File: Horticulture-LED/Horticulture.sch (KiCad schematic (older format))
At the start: 66 parts, among them J3 Conn_01x04_Male, J4 Conn_01x04_Male, U1 TLE4309, U2 TLE4309, U3 TLE4309, U4 TLE4309, U5 PCA9633DP2

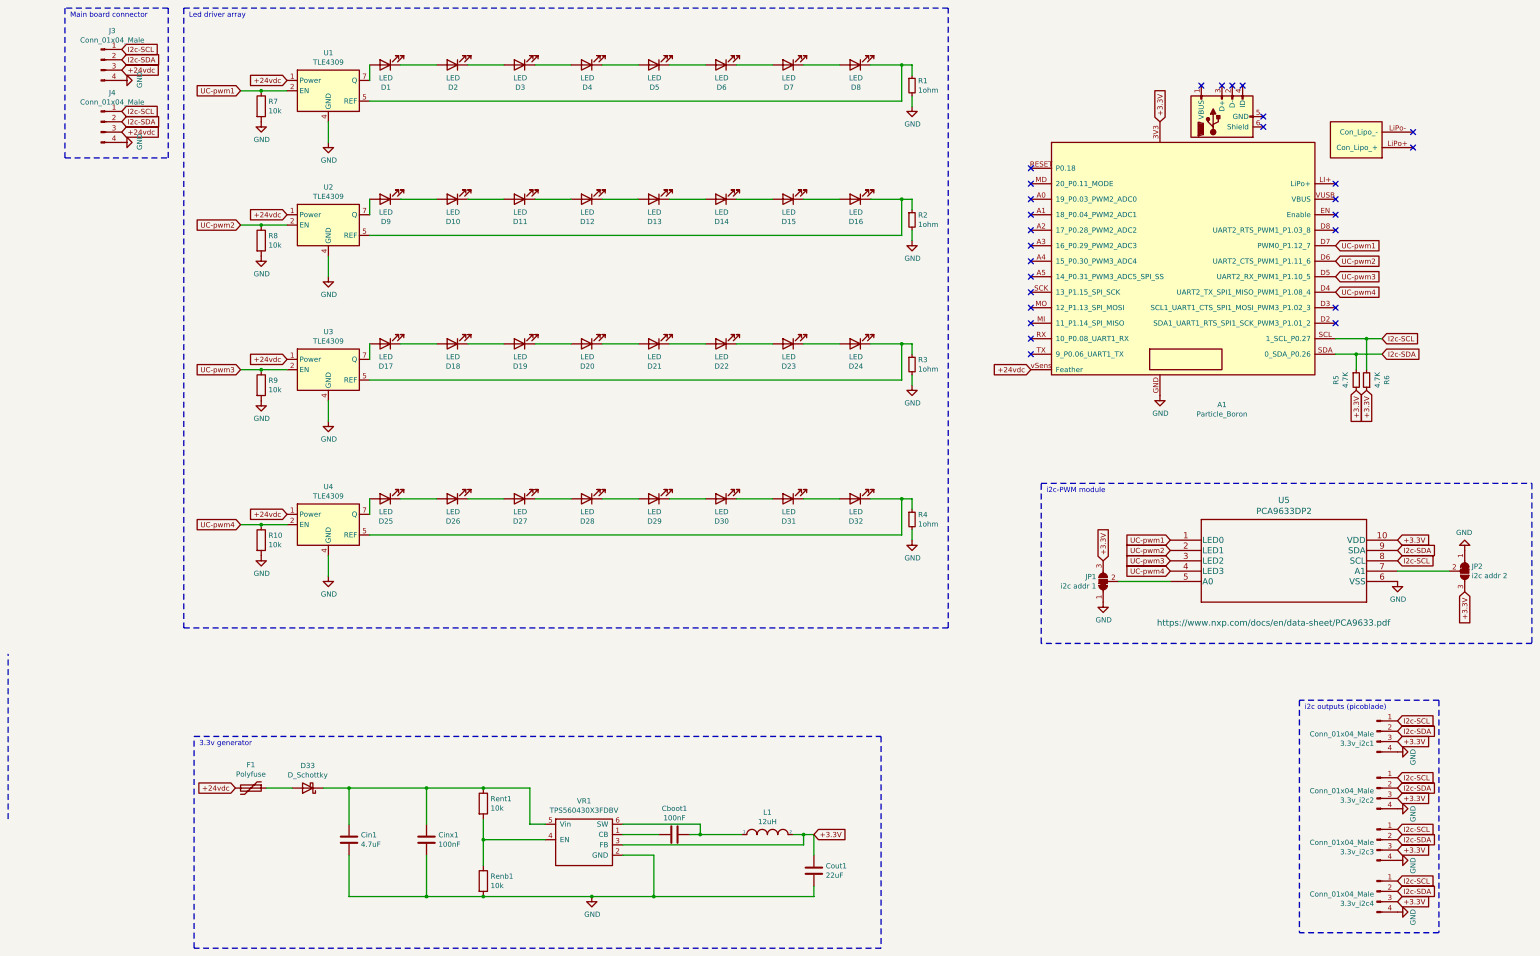
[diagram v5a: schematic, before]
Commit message: ryddet i resistorer
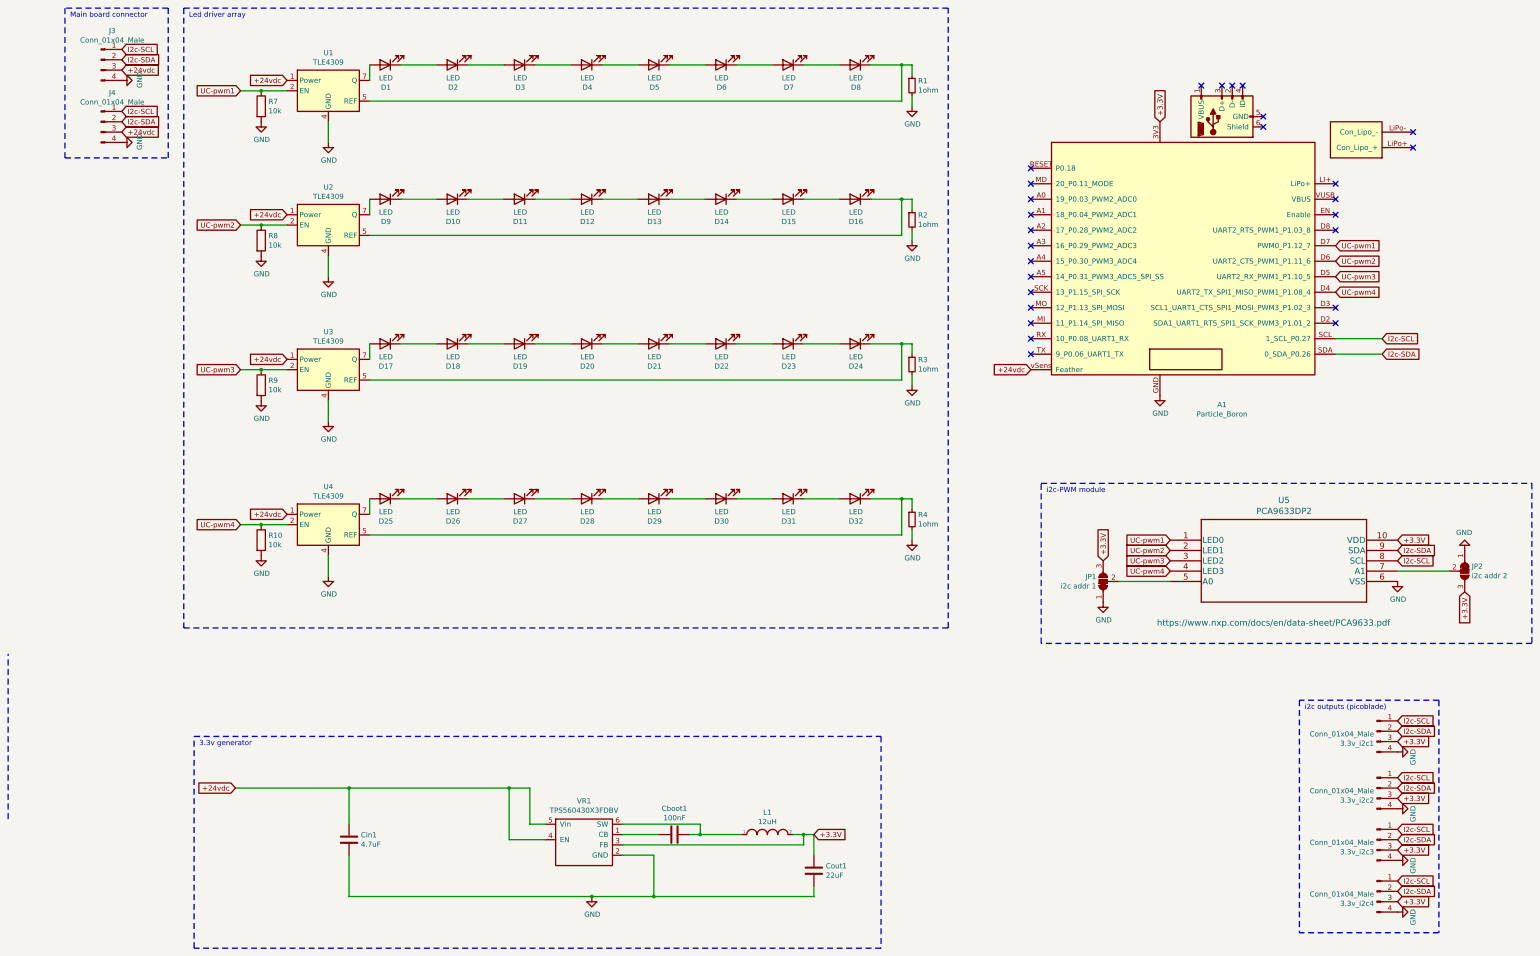
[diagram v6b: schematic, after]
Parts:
- removed Cinx1: 100nF, Capacitor_SMD:C_0603_1608Metric, symbol Device:C
- removed D33: D_Schottky, Diode_SMD:D_SOD-323, symbol Device:D_Schottky
- removed F1: Polyfuse, Fuse:Fuse_1206_3216Metric, symbol Device:Polyfuse
- removed R5, R6: 4.7K, Resistor_SMD:R_0402_1005Metric, symbol Device:R_Small
- removed Renb1, Rent1: 10k, Resistor_SMD:R_0402_1005Metric, symbol Device:R
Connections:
- net +24vdc: now also Cin1.1, VR1.4 (EN), VR1.5 (Vin)
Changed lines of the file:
@@
 Connection ~ 9100 5500
-$Comp
-L particle:Particle_Boron A1
-U 1 1 5EF20E12
-P 11800 3050
-F 0 "A1" H 12200 1511 50  0000 C CNN
-F 1 "Particle_Boron" H 12200 1420 50  0000 C CNN
-F 2 "Adafruit_FeatherWing:PCB_FeatherWing" H 11100 3250 50  0001 C CNN
-F 3 "" H 11100 3250 50  0001 C CNN
-	1    11800 3050
-	1    0    0    -1
-$EndComp
 $Comp
 L Connector:Conn_01x04_Male J3
@@
 +3.3V
 $Comp
-L Device:R_Small R5
-U 1 1 5F25CC3B
-P 13500 4350
-F 0 "R5" V 13304 4350 50  0000 C CNN
-F 1 "4.7K" V 13395 4350 50  0000 C CNN
-F 2 "Resistor_SMD:R_0402_1005Metric" H 13500 4350 50  0001 C CNN
-F 3 "~" H 13500 4350 50  0001 C CNN
-	1    13500 4350
-	1    0    0    -1
-$EndComp
-$Comp
-L Device:R_Small R6
-U 1 1 5F25F078
-P 13600 4350
-F 0 "R6" V 13404 4350 50  0000 C CNN
-F 1 "4.7K" V 13495 4350 50  0000 C CNN
-F 2 "Resistor_SMD:R_0402_1005Metric" H 13600 4350 50  0001 C CNN
-F 3 "~" H 13600 4350 50  0001 C CNN
-	1    13600 4350
-	-1   0    0    1
-$EndComp
-Wire Wire Line
-	13600 4250 13600 3950
-Connection ~ 13600 3950
-Wire Wire Line
-	13600 3950 13750 3950
-Wire Wire Line
-	13500 4250 13500 4100
-Connection ~ 13500 4100
-Wire Wire Line
-	13500 4100 13750 4100
-Text GLabel 13500 4450 3    50   Input ~ 0
-+3.3V
-Text GLabel 13600 4450 3    50   Input ~ 0
-+3.3V
-$Comp
 L Connector:Conn_01x04_Male J4
 U 1 1 5F2EA6B4
@@
 Text GLabel 8250 8750 2    50   Input ~ 0
 +3.3V
-Connection ~ 5050 8800
-Wire Wire Line
-	5050 8800 5050 9050
-Wire Wire Line
-	5050 8600 5050 8800
-Wire Wire Line
-	5650 8800 5050 8800
 Wire Wire Line
 	6700 9350 8250 9350
@@
 Wire Wire Line
 	8050 8750 8150 8750
-Connection ~ 5050 9350
 Wire Wire Line
 	8250 9350 8250 9250
 Wire Wire Line
-	5050 9350 6100 9350
-Wire Wire Line
 	7050 8750 7150 8750
 Wire Wire Line
-	4500 9350 3750 9350
-Connection ~ 4500 9350
-Wire Wire Line
-	4500 8950 4500 9350
-Wire Wire Line
 	3750 9350 3750 8950
 Wire Wire Line
-	5050 9350 4500 9350
-Wire Wire Line
-	4500 8300 3750 8300
-Connection ~ 4500 8300
-Wire Wire Line
-	4500 8650 4500 8300
-Connection ~ 5050 8300
-Wire Wire Line
 	3750 8300 3750 8650
 Wire Wire Line
-	5050 8300 4500 8300
-Wire Wire Line
-	5500 8300 5050 8300
+	5500 8300 5300 8300
 Wire Wire Line
 	5500 8650 5500 8300
 Wire Wire Line
 	5650 8650 5500 8650
-$Comp
-L Device:R Renb1
-U 1 1 5F7D2821
-P 5050 9200
-F 0 "Renb1" H 5120 9246 50  0000 L CNN
-F 1 "10k" H 5120 9155 50  0000 L CNN
-F 2 "Resistor_SMD:R_0402_1005Metric" V 4980 9200 50  0001 C CNN
-F 3 "~" H 5050 9200 50  0001 C CNN
-	1    5050 9200
-	1    0    0    -1
-$EndComp
-$Comp
-L Device:R Rent1
-U 1 1 5F7D0EBB
-P 5050 8450
-F 0 "Rent1" H 5120 8496 50  0000 L CNN
-F 1 "10k" H 5120 8405 50  0000 L CNN
-F 2 "Resistor_SMD:R_0402_1005Metric" V 4980 8450 50  0001 C CNN
-F 3 "~" H 5050 8450 50  0001 C CNN
-	1    5050 8450
-	1    0    0    -1
-$EndComp
 $Comp
 L pspice:INDUCTOR L1
@@
 $EndComp
 $Comp
-L Device:C Cinx1
-U 1 1 5F7BFD6B
-P 4500 8800
-F 0 "Cinx1" H 4615 8846 50  0000 L CNN
-F 1 "100nF" H 4615 8755 50  0000 L CNN
-F 2 "Capacitor_SMD:C_0603_1608Metric" H 4538 8650 50  0001 C CNN
-F 3 "~" H 4500 8800 50  0001 C CNN
-	1    4500 8800
-	1    0    0    -1
-$EndComp
-$Comp
 L Device:C Cin1
 U 1 1 5F7BEDEC
@@
 Wire Notes Line
 	450  8600 450  7000
-$Comp
-L Device:Polyfuse F1
-U 1 1 5F8B0FBE
-P 2800 8300
-F 0 "F1" V 2575 8300 50  0000 C CNN
-F 1 "Polyfuse" V 2666 8300 50  0000 C CNN
-F 2 "Fuse:Fuse_1206_3216Metric" H 2850 8100 50  0001 L CNN
-F 3 "~" H 2800 8300 50  0001 C CNN
-	1    2800 8300
-	0    1    1    0
-$EndComp
-$Comp
-L Device:D_Schottky D33
-U 1 1 5F8B2DE3
-P 3350 8300
-F 0 "D33" H 3350 8083 50  0000 C CNN
-F 1 "D_Schottky" H 3350 8174 50  0000 C CNN
-F 2 "Diode_SMD:D_SOD-323" H 3350 8300 50  0001 C CNN
-F 3 "~" H 3350 8300 50  0001 C CNN
-	1    3350 8300
-	-1   0    0    1
-$EndComp
-Wire Wire Line
-	2950 8300 3200 8300
-Wire Wire Line
-	3500 8300 3750 8300
 Connection ~ 3750 8300
 $Comp
@@
 NoConn ~ 10350 2750
 NoConn ~ 10350 2900
-Wire Wire Line
-	13300 4100 13500 4100
-Wire Wire Line
-	13300 3950 13600 3950
 Text GLabel 13900 8200 2    50   Input ~ 0
 I2c-SCL
@@
 	1    0    0    -1
 $EndComp
+Wire Wire Line
+	5300 8300 5300 8800
+Connection ~ 5300 8300
+Wire Wire Line
+	5300 8800 5650 8800
+Wire Wire Line
+	2650 8300 3750 8300
+$Comp
+L particle:Particle_Boron A1
+U 1 1 5EF20E12
+P 11800 3050
+F 0 "A1" H 12200 1511 50  0000 C CNN
+F 1 "Particle_Boron" H 12200 1420 50  0000 C CNN
+F 2 "Adafruit_FeatherWing:PCB_FeatherWing" H 11100 3250 50  0001 C CNN
+F 3 "" H 11100 3250 50  0001 C CNN
+	1    11800 3050
+	1    0    0    -1
+$EndComp
+Wire Wire Line
+	13300 4100 13750 4100
+Wire Wire Line
+	13300 3950 13750 3950
+Wire Wire Line
+	3750 9350 6100 9350
+Wire Wire Line
+	3750 8300 5300 8300
 $EndSCHEMATC

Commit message: Satt Farge på LED
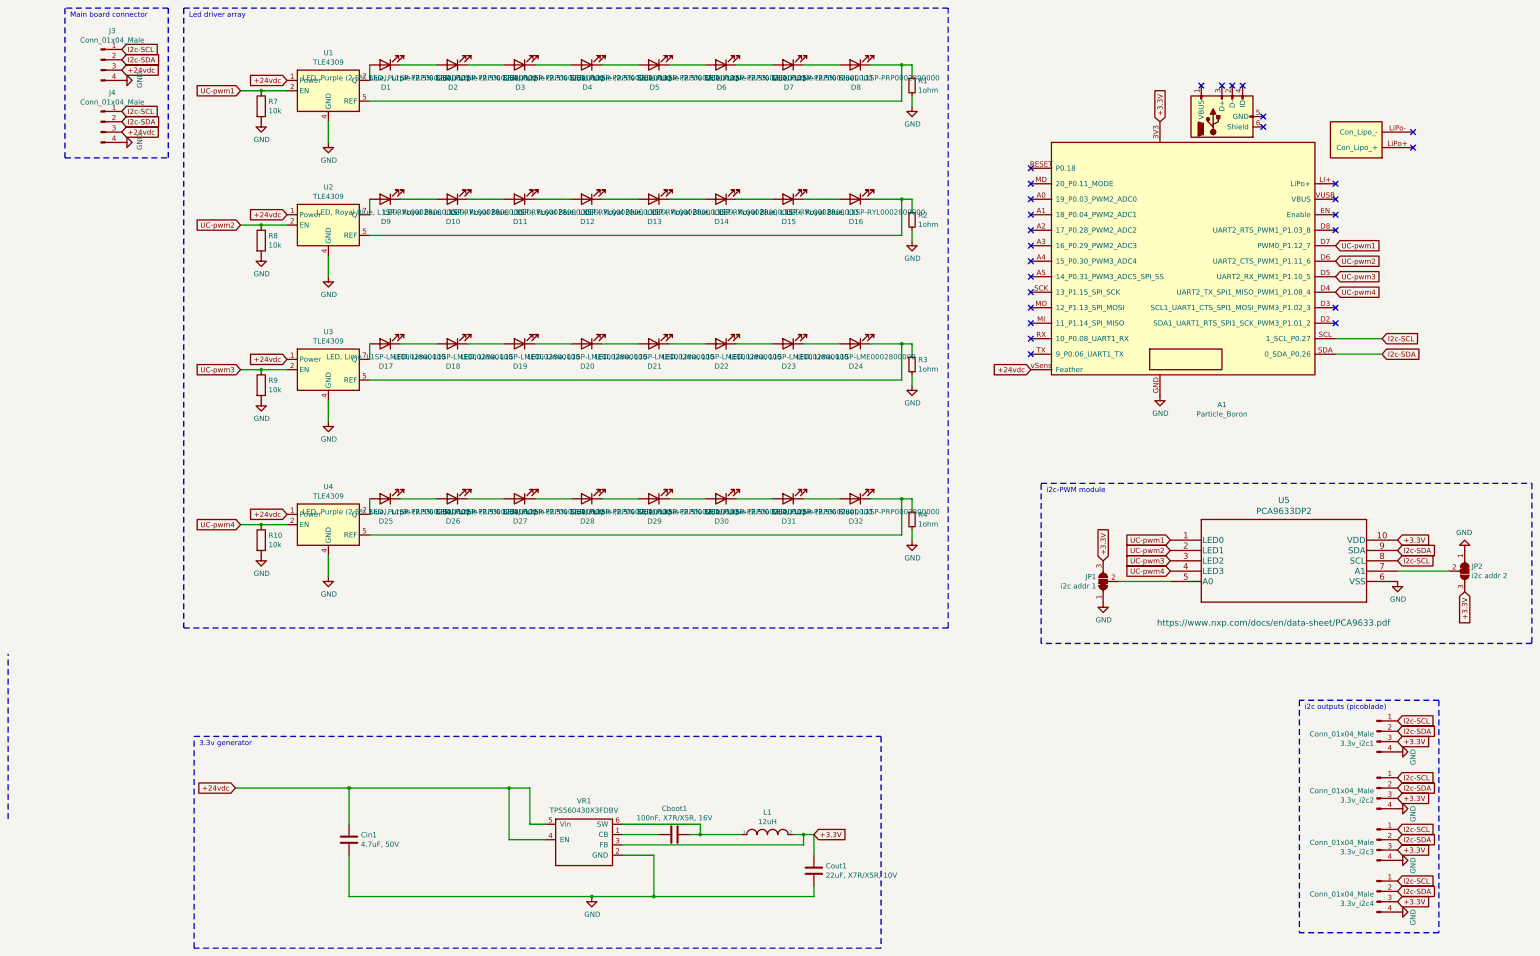
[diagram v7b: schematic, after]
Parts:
- Cboot1: value 100nF -> 100nF, X7R/X5R, 16V
- Cin1: value 4.7uF -> 4.7uF, 50V
- Cout1: value 22uF -> 22uF, X7R/X5R, 10V
- D1, D2, D25, D26, D27, D28, D29, D3, D30, D31, D32, D4, D5, D6, D7, D8: value LED -> LED, Purple (2.5% Blue), L1SP-PRP0002800000
- D10, D11, D12, D13, D14, D15, D16, D9: value LED -> LED, Royal Blue, L1SP-RYL0002800000
- D17, D18, D19, D20, D21, D22, D23, D24: value LED -> LED, Lime, L1SP-LME0002800000

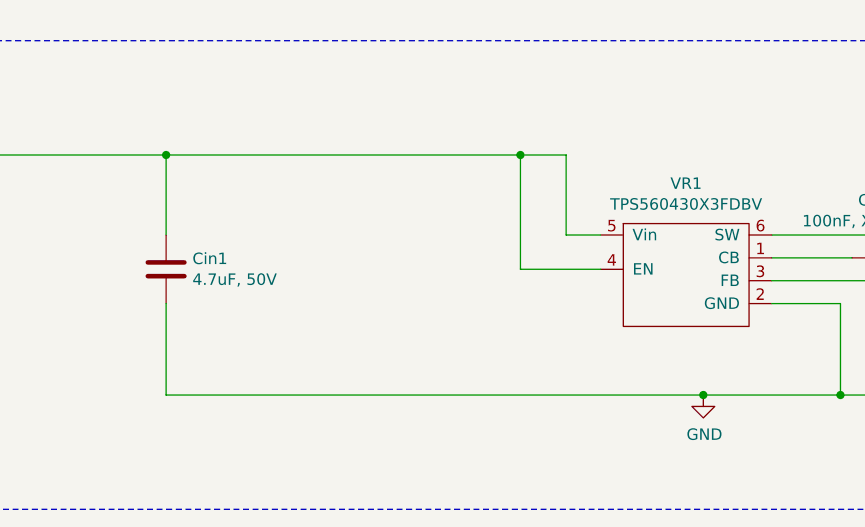
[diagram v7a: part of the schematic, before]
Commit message: fixes #10 #11 #12
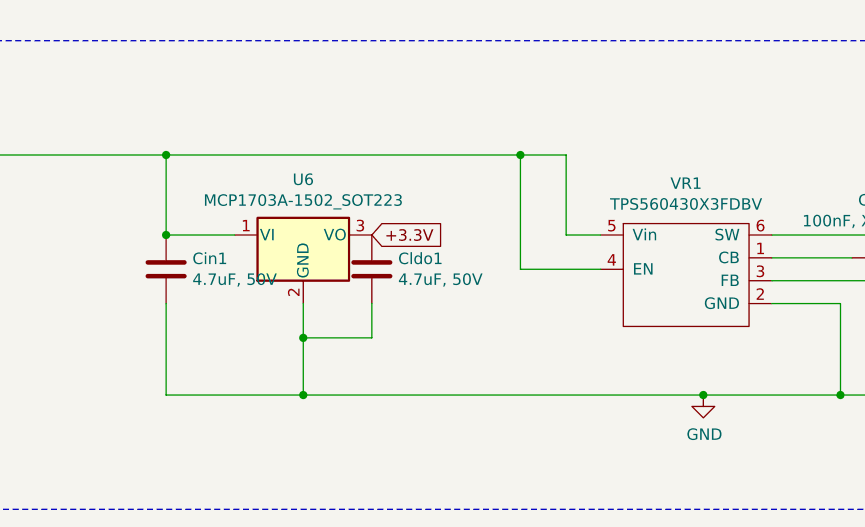
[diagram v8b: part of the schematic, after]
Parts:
- added Cldo1: 4.7uF, 50V, Capacitor_SMD:C_1206_3216Metric, symbol Device:C
- added U6: MCP1703A-1502_SOT223, Package_TO_SOT_SMD:SOT-223-3_TabPin2, symbol Regulator_Linear:MCP1703A-1502_SOT223
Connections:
- net +24vdc: now also U6.1 (VI)
- net +3.3V: now also Cldo1.1, U6.3 (VO)
- net GND: now also Cldo1.2, U6.2 (GND)
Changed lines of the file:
@@
 	13300 3950 13750 3950
 Wire Wire Line
-	3750 9350 6100 9350
+	3750 9350 4350 9350
 Wire Wire Line
 	3750 8300 5300 8300
+$Comp
+L Regulator_Linear:MCP1703A-1502_SOT223 U6
+U 1 1 6127D649
+P 4350 8650
+F 0 "U6" H 4350 8892 50  0000 C CNN
+F 1 "MCP1703A-1502_SOT223" H 4350 8801 50  0000 C CNN
+F 2 "Package_TO_SOT_SMD:SOT-223-3_TabPin2" H 4350 8850 50  0001 C CNN
+F 3 "http://ww1.microchip.com/downloads/en/DeviceDoc/20005122B.pdf" H 4350 8600 50  0001 C CNN
+	1    4350 8650
+	1    0    0    -1
+$EndComp
+Wire Wire Line
+	4050 8650 3750 8650
+Connection ~ 3750 8650
+Wire Wire Line
+	4350 8950 4350 9100
+Connection ~ 4350 9350
+Wire Wire Line
+	4350 9350 6100 9350
+$Comp
+L Device:C Cldo1
+U 1 1 61285EC2
+P 4650 8800
+F 0 "Cldo1" H 4765 8846 50  0000 L CNN
+F 1 "4.7uF, 50V" H 4765 8755 50  0000 L CNN
+F 2 "Capacitor_SMD:C_1206_3216Metric" H 4688 8650 50  0001 C CNN
+F 3 "~" H 4650 8800 50  0001 C CNN
+	1    4650 8800
+	1    0    0    -1
+$EndComp
+Wire Wire Line
+	4650 8950 4650 9100
+Wire Wire Line
+	4650 9100 4350 9100
+Connection ~ 4350 9100
+Wire Wire Line
+	4350 9100 4350 9350
+Text GLabel 4650 8650 2    50   Input ~ 0
++3.3V
 $EndSCHEMATC
